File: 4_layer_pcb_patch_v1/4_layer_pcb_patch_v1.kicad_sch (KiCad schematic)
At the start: 1 part, among them J1 Conn_Coaxial_Small

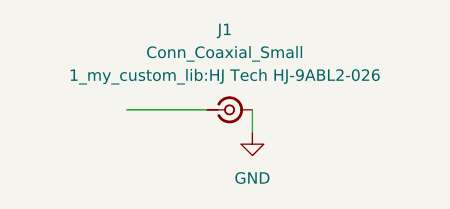
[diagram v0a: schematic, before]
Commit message: Ground vias adjusted
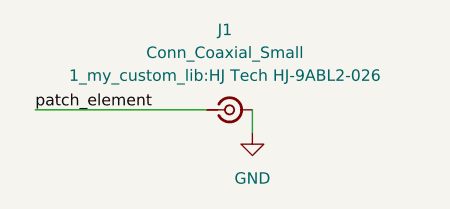
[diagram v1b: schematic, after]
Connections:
- net patch_element: now reaches J1.1 (In)
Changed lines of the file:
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@@
 	(wire
 		(pts
-			(xy 120.65 133.35) (xy 129.54 133.35)
+			(xy 110.49 133.35) (xy 129.54 133.35)
 		)
 		(stroke
@@
 		)
 	)
-	(netclass_flag ""
-		(length 2.54)
-		(shape round)
-		(at 120.65 133.35 0)
+	(label "patch_element"
+		(at 110.49 133.35 0)
 		(fields_autoplaced yes)
 		(effects
@@
 			(justify left bottom)
 		)
-		(property "Netclass" ""
-			(at 121.3485 130.81 0)
-			(effects
-				(font
-					(size 1.27 1.27)
-					(italic yes)
-				)
-				(justify left)
-			)
-		)
 	)
